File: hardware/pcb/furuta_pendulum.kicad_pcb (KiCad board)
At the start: 4 copper layers, 72 parts, among them J2 LCD_ST7735S, J3 DRV8313, J4 SWD, J7 Encoders, J8 USB_C_Receptacle_USB2.0_14P, SW1 TS-1088-AR02016, SW2 TS-1088-AR02016, U1 AMS1117-3.3, U3 USBLC6-2SC6, U7 ATSAMD51J20A-A

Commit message: Add PCB layout file and project local settings
Co-authored-by: Copilot <223556219+Copilot@users.noreply.github.com>
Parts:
- moved FID1 32.9 mm to (87.5, 59.9)
- moved FID2 32.9 mm to (87.5, 63.4)
- moved FID3 32.9 mm to (87.5, 67.0)
- moved H1 32.9 mm to (81.8, 62.1)
- moved H2 32.9 mm to (81.8, 70.0)
- moved H3 32.9 mm to (81.8, 78.0)
- moved H4 32.9 mm to (81.8, 85.9)
- moved J2 11.7 mm to (152.6, 90.7)
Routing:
- net /VDDCORE: track 0.00 -> 3.99 mm
- net /VDDIO: track 20.1 -> 22.1 mm
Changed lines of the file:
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@@
 	(footprint "Fiducial:Fiducial_1mm_Mask2mm"
 		(layer "F.Cu")
-		(at 54.9 62.95)
+		(at 87.538 66.978)
 		(descr "Fiducial, circular marking, 1mm bare copper, 2mm soldermask opening (Level A)")
 		(tags "fiducial")
@@
 	(footprint "Fiducial:Fiducial_1mm_Mask2mm"
 		(layer "F.Cu")
-		(at 54.9 55.85)
+		(at 87.538 59.878)
 		(descr "Fiducial, circular marking, 1mm bare copper, 2mm soldermask opening (Level A)")
 		(tags "fiducial")
@@
 	(footprint "MountingHole:MountingHole_2.2mm_M2"
 		(layer "F.Cu")
-		(at 49.15 58.05)
+		(at 81.788 62.078)
 		(descr "Mounting Hole 2.2mm, M2, no annular, generated by kicad-footprint-generator mountinghole.py")
 		(tags "mountinghole M2")
@@
 	(footprint "MountingHole:MountingHole_2.2mm_M2"
 		(layer "F.Cu")
-		(at 49.15 66)
+		(at 81.788 70.028)
 		(descr "Mounting Hole 2.2mm, M2, no annular, generated by kicad-footprint-generator mountinghole.py")
 		(tags "mountinghole M2")
@@
 	(footprint "MountingHole:MountingHole_2.2mm_M2"
 		(layer "F.Cu")
-		(at 49.15 73.95)
+		(at 81.788 77.978)
 		(descr "Mounting Hole 2.2mm, M2, no annular, generated by kicad-footprint-generator mountinghole.py")
 		(tags "mountinghole M2")
@@
 	(footprint "Connector_PinHeader_2.54mm:PinHeader_2x04_P2.54mm_Vertical"
 		(layer "F.Cu")
-		(at 160.269 81.788)
+		(at 152.649 90.678)
 		(descr "Through hole straight pin header, 2x04, 2.54mm pitch, double rows")
 		(tags "Through hole pin header THT 2x04 2.54mm double row")
@@
 	(footprint "Fiducial:Fiducial_1mm_Mask2mm"
 		(layer "F.Cu")
-		(at 54.9 59.4)
+		(at 87.538 63.428)
 		(descr "Fiducial, circular marking, 1mm bare copper, 2mm soldermask opening (Level A)")
 		(tags "fiducial")
@@
 	(footprint "MountingHole:MountingHole_2.2mm_M2"
 		(layer "F.Cu")
-		(at 49.15 81.9)
+		(at 81.788 85.928)
 		(descr "Mounting Hole 2.2mm, M2, no annular, generated by kicad-footprint-generator mountinghole.py")
 		(tags "mountinghole M2")
@@
 	)
 	(segment
+		(start 132.588 83.312)
+		(end 132.616 83.34)
+		(width 0.2)
+		(layer "F.Cu")
+		(net "/VDDCORE")
+	)
+	(segment
+		(start 132.093 82.509)
+		(end 132.052 82.55)
+		(width 0.5)
+		(layer "F.Cu")
+		(net "/VDDCORE")
+	)
+	(segment
+		(start 132.052 82.55)
+		(end 132.052 82.776)
+		(width 0.5)
+		(layer "F.Cu")
+		(net "/VDDCORE")
+	)
+	(segment
+		(start 132.093 81.026)
+		(end 132.093 82.509)
+		(width 0.5)
+		(layer "F.Cu")
+		(net "/VDDCORE")
+	)
+	(segment
+		(start 134.0375 83.34)
+		(end 132.616 83.34)
+		(width 0.2)
+		(layer "F.Cu")
+		(net "/VDDCORE")
+	)
+	(segment
+		(start 132.052 82.776)
+		(end 132.588 83.312)
+		(width 0.5)
+		(layer "F.Cu")
+		(net "/VDDCORE")
+	)
+	(segment
 		(start 132.334 84.074)
 		(end 132.588 84.328)
@@
 	)
 	(segment
+		(start 143.576 77.216)
+		(end 143.576 75.908)
+		(width 0.5)
+		(layer "F.Cu")
+		(net "/VDDIO")
+	)
+	(segment
 		(start 143.002 77.79)
 		(end 143.002 78.232)
@@
 		(layer "F.Cu")
 		(net "/VDDIO")
+	)
+	(segment
+		(start 143.576 75.908)
+		(end 144.046 75.438)
+		(width 0.5)
+		(layer "F.Cu")
+		(net "/VDDIO")

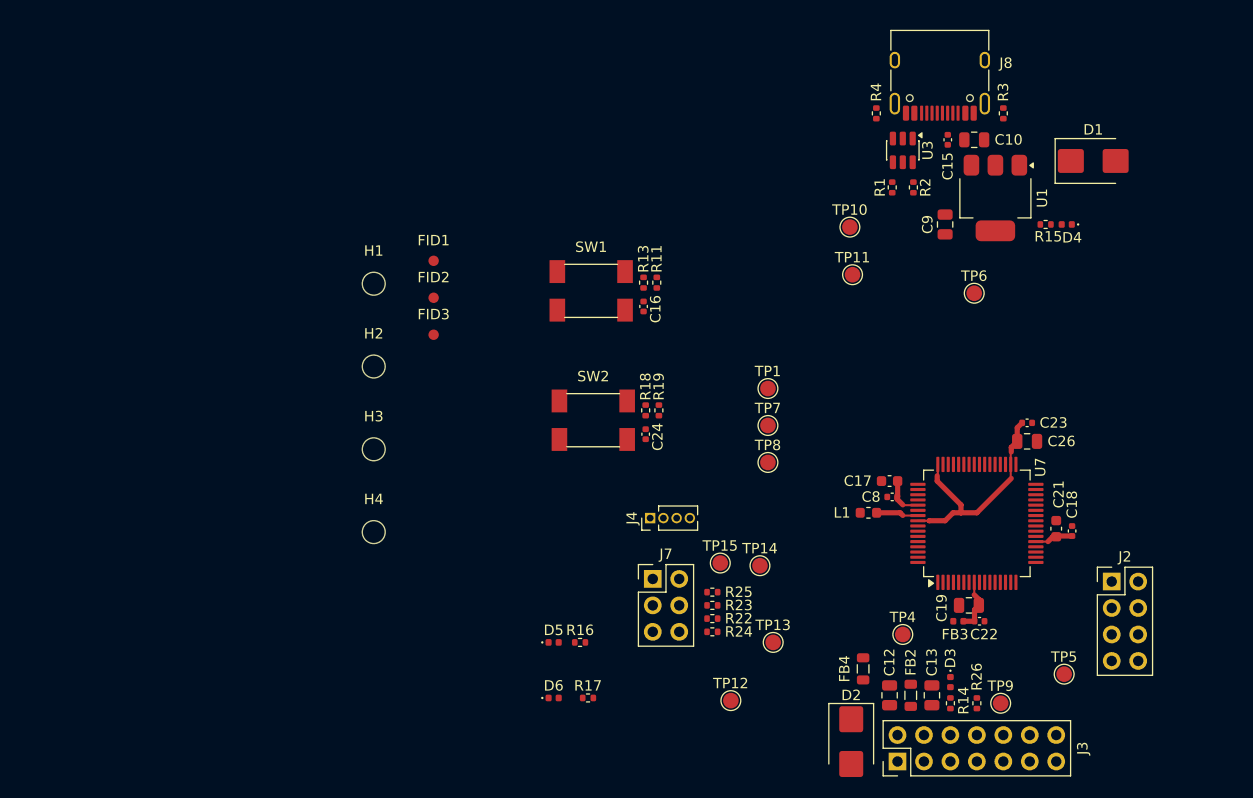
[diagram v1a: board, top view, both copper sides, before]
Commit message: PCB Rev 1 — production release to JLCPCB
Includes final schematic and layout changes, production files (Gerbers,
BOM, positions), JLCPCB component mapping, Claude Code project instructions
and MCP config, and component datasheet.

Co-Authored-By: Claude Sonnet 4.6 <noreply@anthropic.com>
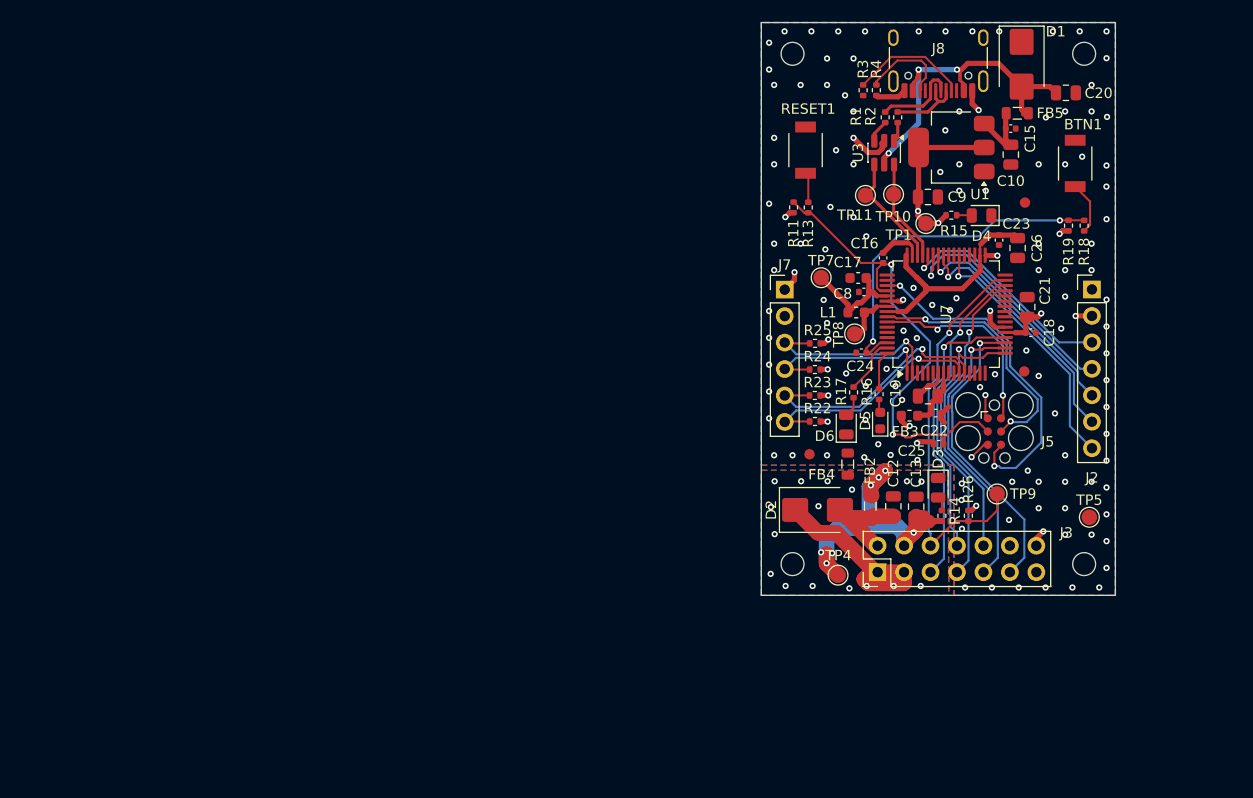
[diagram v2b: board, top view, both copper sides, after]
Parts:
- removed J4: SWD, Connector_PinHeader_1.27mm:PinHeader_1x04_P1.27mm_Vertical
- removed TP12, TP13, TP14, TP15, TP6: TestPoint, TestPoint:TestPoint_Pad_D1.5mm
- added C20: 10u, Capacitor_SMD:C_0805_2012Metric, F.Cu at (148.2, 43.8)
- added C25: 100n, Capacitor_SMD:C_0402_1005Metric, F.Cu at (136.0, 77.5)
- added FB5: GZ2012D601TF, Inductor_SMD:L_0805_2012Metric, F.Cu at (143.6, 45.7)
- added J5: Conn_ARM_SWD_TagConnect_TC2030, Connector:Tag-Connect_TC2030-IDC-FP_2x03_P1.27mm_Vertical, F.Cu at (141.4, 76.3)
- C21: footprint Capacitor_SMD:C_0603_1608Metric -> Capacitor_SMD:C_0805_2012Metric
- D1: value SMBJ15A -> SMBJ5.0A
- D2: value SMBJ5.0A -> SMBJ12A
- D3, D4: footprint LED_SMD:LED_0402_1005Metric -> LED_SMD:LED_0805_2012Metric
- D5: footprint LED_SMD:LED_0402_1005Metric -> LED_SMD:LED_0603_1608Metric
- D6: value BLUE -> YELLOW; footprint LED_SMD:LED_0402_1005Metric -> LED_SMD:LED_0805_2012Metric
- FB2: value BLM21PG121SN1L -> GZ2012D601TF
- FB3: footprint Inductor_SMD:L_0402_1005Metric -> Inductor_SMD:L_0603_1608Metric
- FB4: value BLM21PG121SN1L -> GZ2012D101TF
- J2: footprint Connector_PinHeader_2.54mm:PinHeader_2x04_P2.54mm_Vertical -> Connector_PinHeader_2.54mm:PinHeader_1x07_P2.54mm_Vertical
- J7: footprint Connector_PinHeader_2.54mm:PinHeader_2x03_P2.54mm_Vertical -> Connector_PinHeader_2.54mm:PinHeader_1x06_P2.54mm_Vertical
- R1, R2: value 27 -> 33
- R17: value 500 -> 1k
- moved H2 74.5 mm to (150.0, 40.0)
- moved H4 68.3 mm to (150.0, 89.0)
- moved FID1 57.7 mm to (144.2, 70.5)
- moved FID2 57.5 mm to (144.3, 54.3)
- moved BTN1 52.4 mm to (149.1, 50.5), turned to 90 degrees
- moved H1 45.9 mm to (122.0, 40.0)
- moved R18 45.7 mm to (150.0, 56.5), turned to 90 degrees
- moved R19 43.1 mm to (148.5, 56.5), turned to -90 degrees
- moved H3 41.7 mm to (122.0, 89.0)
- moved R17 38.9 mm to (127.9, 72.5), turned to -90 degrees
- moved D6 38.4 mm to (127.2, 75.6), turned to 90 degrees
- moved D5 37.9 mm to (130.4, 75.2), turned to 90 degrees
- moved FID3 37.9 mm to (123.6, 78.5)
- moved R16 37.3 mm to (130.3, 72.7), turned to -90 degrees
- moved J7 30.5 mm to (121.2, 62.6)
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- renumbered SW2 to BTN1, SW1 to RESET1
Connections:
- D1 pad 1: +5V -> GND
- D1 pad 2: GND -> VBUS
- D2 pad 1: +12V -> PGND
- D2 pad 2: PGND -> +12V
- J7 pad 4: /I2C_PENDULUM_SCL -> /I2C_ARM_SDA
- J7 pad 5: /I2C_ARM_SDA -> /I2C_PENDULUM_SCL
- J8 pad A4: +5V -> VBUS
- J8 pad A9: +5V -> VBUS
- J8 pad B4: +5V -> VBUS
- J8 pad B9: +5V -> VBUS
- J8 pad SH: unconnected-(J8-SHIELD-PadSH)_2 -> /unconnected-(J8-SHIELD-PadSH)_2_2
- L1 pad 1: GND -> /VDDCORE
- R1 pad 1: /MCU_D+ -> /ESD_D+
- R1 pad 2: /ESD_D+ -> /USB_D+
- R2 pad 1: /ESD_D- -> /USB_D-
- R2 pad 2: /MCU_D- -> /ESD_D-
- U3 pad 1: /USB_D- -> /ESD_D-
- U3 pad 3: /USB_D+ -> /ESD_D+
- U3 pad 4: /ESD_D+ -> /MCU_D+
- U3 pad 5: +5V -> VBUS
- U3 pad 6: /ESD_D- -> /MCU_D-
- U7 pad 51: unconnected-(U7-PA27-Pad51) -> Net-(J5-SWO)
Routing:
- net /MCU_RESET: track 0.00 -> 46.1 mm, vias 0 -> 2
- net /DRV_FAULT: track 0.00 -> 38.6 mm, vias 0 -> 1
- net VBUS: track 0.00 -> 35.7 mm, vias 0 -> 3
- net GND: track 0.00 -> 35.1 mm, vias 0 -> 126
- net +3.3V: track 3.74 -> 37.3 mm, vias 0 -> 15
- net /MCU_SW2: track 0.00 -> 33.4 mm, vias 0 -> 2
- net Net-(J5-SWO): track 0.00 -> 32.8 mm, vias 0 -> 2
- net +12VF: track 0.00 -> 31.4 mm, vias 0 -> 7
- net /DRV_ENABLE: track 0.00 -> 29.2 mm, vias 0 -> 1
- net /DRV_PWM3: track 0.00 -> 29.0 mm, vias 0 -> 1
- net /DRV_SLEEP: track 0.00 -> 28.9 mm, vias 0 -> 1
- net /DRV_PWM1: track 0.00 -> 28.9 mm, vias 0 -> 1
- net /DRV_RESET: track 0.00 -> 28.8 mm, vias 0 -> 1
- net /DRV_PWM2: track 0.00 -> 28.1 mm, vias 0 -> 1
- net /LCD_RST: track 0.00 -> 24.8 mm, vias 0 -> 1
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- added copper zone on In2.Cu, net +12VF
- added copper zone on In2.Cu, net +3.3V
- added copper zone on B.Cu, net GND
- added copper zone on F.Cu, net GND
- added copper zone on In1.Cu, net GND
- added copper zone on B.Cu, net PGND
- added copper zone on F.Cu, net PGND
- added copper zone on In1.Cu, net PGND
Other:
- board outline added: 34 x 55 mm
- board text added: "Furuta Pendulum Control Board"
- board text added: "Rev 1, 06/26 By: Morten Vandborg"
